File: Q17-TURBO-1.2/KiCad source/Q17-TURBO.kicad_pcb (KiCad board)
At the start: 2 copper layers, 190 x 75 mm, 106 parts, among them J1 INPUT, J2 SPK+, J3 DC, Q1 IRF610, Q10 KSA992, Q12 KSC1845, Q13 IRF610, Q14 IRF9610, Q15 FQA46N15, Q16 IXTH48P20P, Q17 FQA46N15, Q18 IXTH48P20P, Q2 KSA992, Q3 KSC1845, Q4 IRF9610, Q5 FQPF7P20, Q6 2SK3564, Q7 LSK170B, Q7' DN2540N8-G, Q8 DN2540, Q9 BS250P, T1 TestPoint_THTPad_D1.5mm_Drill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, T2 TestPoint_THTPad_D1.5mm_Drill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, T3 TestPoint_THTPad_D1.5mm_Drill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, T4 TestPoint_THTPad_D1.5mm_Drill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, T5 TestPoint_THTPad_D1.5mm_Drill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, T6 TestPoint_THTPad_D1.5mm_Drill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, U1 OPA1611, U1' OPA1641, U2 NDC7003P

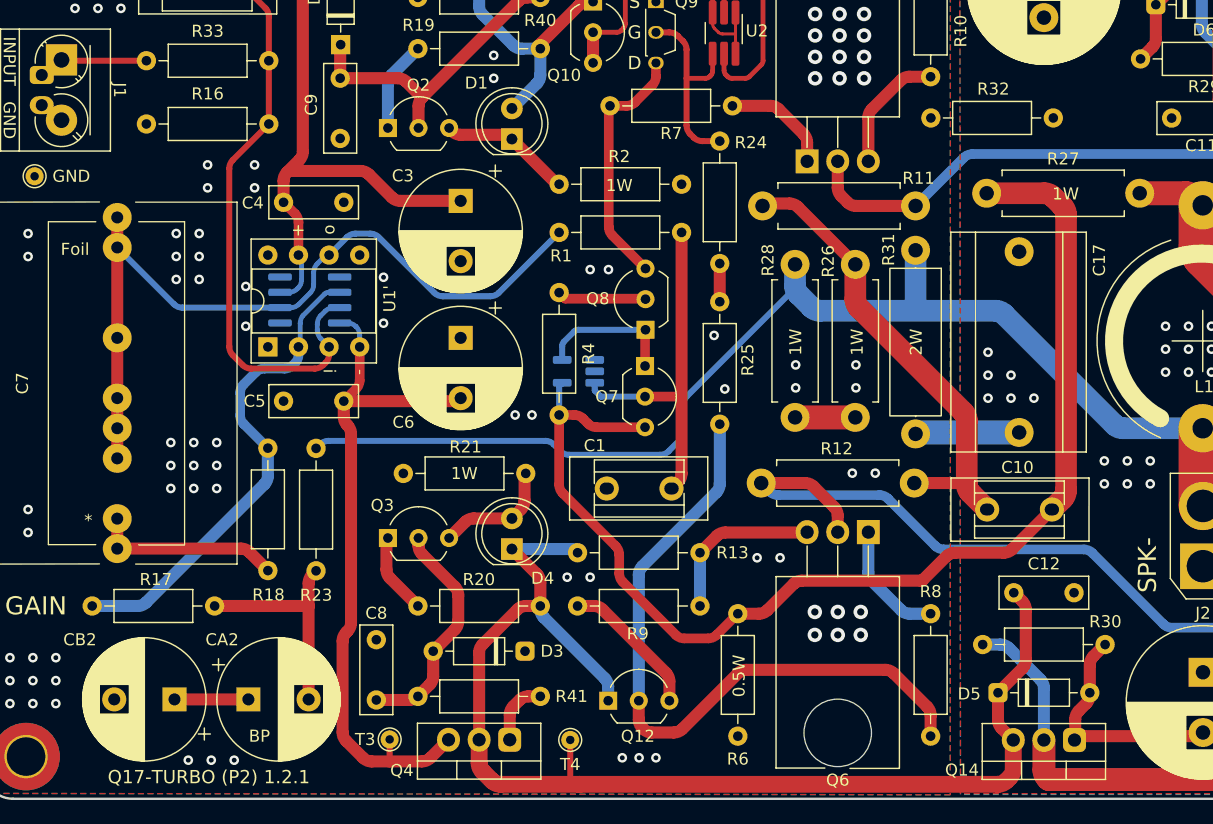
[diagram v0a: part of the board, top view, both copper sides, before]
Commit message: Update Q17-Turbo to 1.2.2
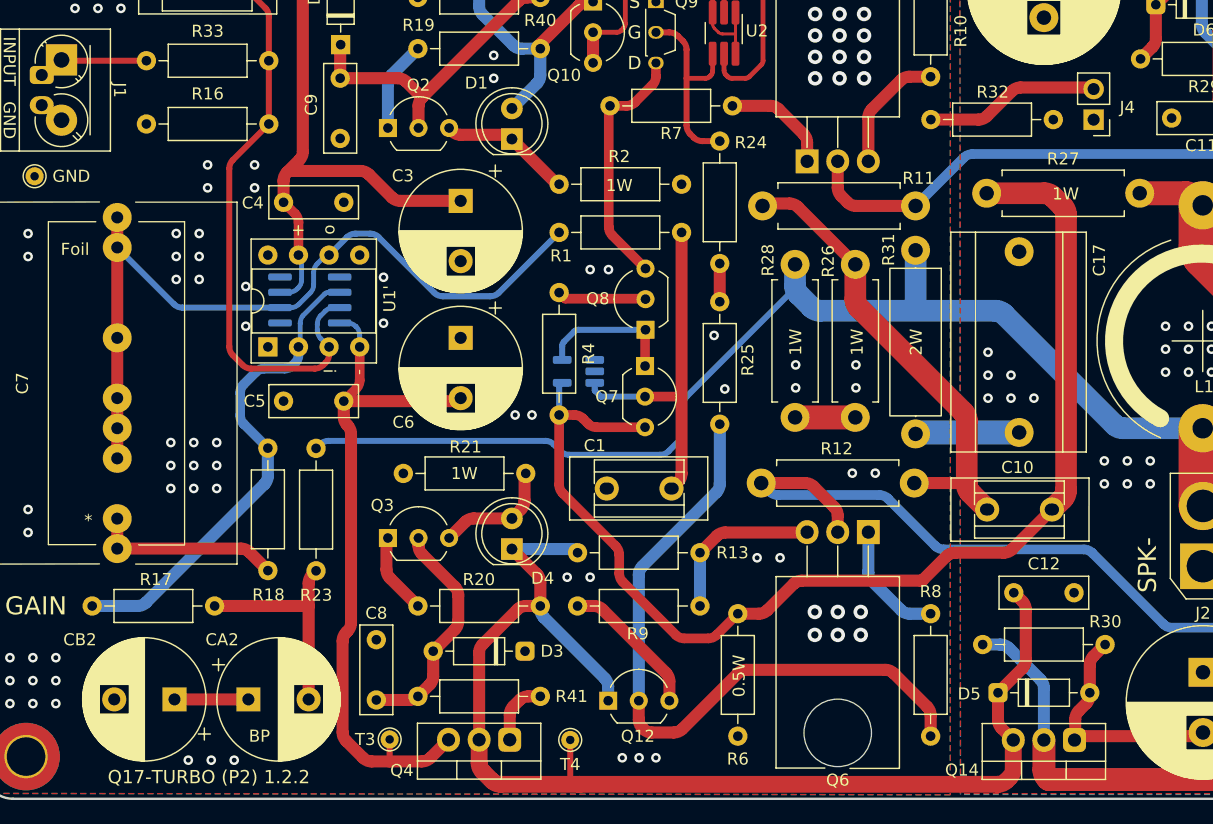
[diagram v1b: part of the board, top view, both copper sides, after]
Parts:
- added J4: PinHeader_1x02_P2.54mm_Vertical, Connector_PinHeader_2.54mm:PinHeader_1x02_P2.54mm_Vertical, F.Cu at (141.2, 89.8)
- moved R32 0.14 mm to (127.7, 89.8)
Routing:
- net GND: track 0.00 -> 14.4 mm
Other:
- board text added: "Q17-TURBO (P2) 1.2.2"
- board text removed: "Q17-TURBO (P2) 1.2.1"
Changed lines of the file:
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@@
   (title_block
     (title "Q17-TURBO (P2)")
-    (date "2023-08-06")
-    (rev "1.2.1")
+    (date "2023-09-04")
+    (rev "1.2.2")
     (company "PCB design by Stef")
     (comment 1 "Zize 190 x 75 mm")
@@
       (drillshape 0)
       (scaleselection 1)
-      (outputdirectory "../Gerber-Q17-TURBO 1.2.1")
+      (outputdirectory "../Gerber-Q17-TURBO 1.2.2")
     )
   )
@@
       (net 44 "Net-(Q4-S)"))
   )
+  (footprint "Connector_PinHeader_2.54mm:PinHeader_1x02_P2.54mm_Vertical" (layer "F.Cu")
+    (at 141.1732 89.7915 180)
+    (descr "Through hole straight pin header, 1x02, 2.54mm pitch, single row")
+    (tags "Through hole pin header THT 1x02 2.54mm single row")
+    (attr through_hole board_only)
+    (fp_text reference "J4" (at -2.794 1.021) (layer "F.SilkS")
+        (effects (font (size 1 1) (thickness 0.15)))
+    )
+    (fp_text value "PinHeader_1x02_P2.54mm_Vertical" (at 0 4.87) (layer "F.Fab")
+        (effects (font (size 1 1) (thickness 0.15)))
+    )
+    (fp_text user "${REFERENCE}" (at 0 1.27 90) (layer "F.Fab")
+        (effects (font (size 1 1) (thickness 0.15)))
+    )
+    (fp_line (start -1.33 -1.33) (end 0 -1.33)
+      (stroke (width 0.12) (type solid)) (layer "F.SilkS"))
+    (fp_line (start -1.33 0) (end -1.33 -1.33)
+      (stroke (width 0.12) (type solid)) (layer "F.SilkS"))
+    (fp_line (start -1.33 1.27) (end -1.33 3.87)
+      (stroke (width 0.12) (type solid)) (layer "F.SilkS"))
+    (fp_line (start -1.33 1.27) (end 1.33 1.27)
+      (stroke (width 0.12) (type solid)) (layer "F.SilkS"))
+    (fp_line (start -1.33 3.87) (end 1.33 3.87)
+      (stroke (width 0.12) (type solid)) (layer "F.SilkS"))
+    (fp_line (start 1.33 1.27) (end 1.33 3.87)
+      (stroke (width 0.12) (type solid)) (layer "F.SilkS"))
+    (fp_line (start -1.8 -1.8) (end -1.8 4.35)
+      (stroke (width 0.05) (type solid)) (layer "F.CrtYd"))
+    (fp_line (start -1.8 4.35) (end 1.8 4.35)
+      (stroke (width 0.05) (type solid)) (layer "F.CrtYd"))
+    (fp_line (start 1.8 -1.8) (end -1.8 -1.8)
+      (stroke (width 0.05) (type solid)) (layer "F.CrtYd"))
+    (fp_line (start 1.8 4.35) (end 1.8 -1.8)
+      (stroke (width 0.05) (type solid)) (layer "F.CrtYd"))
+    (fp_line (start -1.27 -0.635) (end -0.635 -1.27)
+      (stroke (width 0.1) (type solid)) (layer "F.Fab"))
+    (fp_line (start -1.27 3.81) (end -1.27 -0.635)
+      (stroke (width 0.1) (type solid)) (layer "F.Fab"))
+    (fp_line (start -0.635 -1.27) (end 1.27 -1.27)
+      (stroke (width 0.1) (type solid)) (layer "F.Fab"))
+    (fp_line (start 1.27 -1.27) (end 1.27 3.81)
+      (stroke (width 0.1) (type solid)) (layer "F.Fab"))
+    (fp_line (start 1.27 3.81) (end -1.27 3.81)
+      (stroke (width 0.1) (type solid)) (layer "F.Fab"))
+    (pad "1" thru_hole rect (at 0 0 180) (size 1.7 1.7) (drill 1) (layers "*.Cu" "*.Mask")
+      (net 4 "GNDPWR"))
+    (pad "2" thru_hole oval (at 0 2.54 180) (size 1.7 1.7) (drill 1) (layers "*.Cu" "*.Mask")
+      (net 1 "GND"))
+    (model "${KICAD6_3DMODEL_DIR}/Connector_PinHeader_2.54mm.3dshapes/PinHeader_1x02_P2.54mm_Vertical.wrl"
+      (offset (xyz 0 0 0))
+      (scale (xyz 1 1 1))
+      (rotate (xyz 0 0 0))
+    )
+  )
   (footprint "Resistor_THT:R_Axial_DIN0207_L6.3mm_D2.5mm_P10.16mm_Horizontal" (layer "F.Cu")
     (at 98.3472 130.15)
@@
     (descr "Resistor, Axial_DIN0207 series, Axial, Horizontal, pin pitch=10.16mm, 0.25W = 1/4W, length*diameter=6.3*2.5mm^2, http://cdn-reichelt.de/documents/datenblatt/B400/1_4W%23YAG.pdf")
     (tags "Resistor Axial_DIN0207 series Axial Horizontal pin pitch 10.16mm 0.25W = 1/4W length 6.3mm diameter 2.5mm")
-    (property "Mouser" "594-MRS25000C1009FRP")
-    (property "Part#" "MRS25000C1009FRP00")
+    (property "Mouser" "594-MRS2510K00F")
+    (property "Part#" "MRS25000C1002FRP00")
     (property "Sheetfile" "Q17-TURBO.kicad_sch")
     (property "Sheetname" "")
@@
   )
   (footprint "Resistor_THT:R_Axial_DIN0207_L6.3mm_D2.5mm_P10.16mm_Horizontal" (layer "F.Cu")
-    (at 127.6672 89.65)
+    (at 127.6672 89.7865)
     (descr "Resistor, Axial_DIN0207 series, Axial, Horizontal, pin pitch=10.16mm, 0.25W = 1/4W, length*diameter=6.3*2.5mm^2, http://cdn-reichelt.de/documents/datenblatt/B400/1_4W%23YAG.pdf")
     (tags "Resistor Axial_DIN0207 series Axial Horizontal pin pitch 10.16mm 0.25W = 1/4W length 6.3mm diameter 2.5mm")
@@
     (property "ki_keywords" "R res resistor")
     (attr through_hole)
-    (fp_text reference "R32" (at 5.18 -2.4) (layer "F.SilkS")
+    (fp_text reference "R32" (at 5.124 -2.286) (layer "F.SilkS")
         (effects (font (size 1 1) (thickness 0.15)))
     )
@@
     (effects (font (size 1 1) (thickness 0.15)))
   )
-  (gr_text "Q17-TURBO (P2) 1.2.1" (at 67.7472 144.35) (layer "F.SilkS")
+  (gr_text "Q17-TURBO (P2) 1.2.2" (at 67.7472 144.35) (layer "F.SilkS")
     (effects (font (size 1.1 1.1) (thickness 0.2)))
   )
@@
     (effects (font (size 1 1) (thickness 0.15)))
   )
+  (segment (start 141.0437 87.122) (end 135.107914 87.122) (width 1) (layer "F.Cu") (net 1))
+  (segment (start 134.400807 87.414893) (end 132.322093 89.493607) (width 1) (layer "F.Cu") (net 1))
+  (segment (start 131.614986 89.7865) (end 127.6672 89.7865) (width 1) (layer "F.Cu") (net 1))
   (via (at 67.9472 142.945) (size 0.8) (drill 0.4) (layers "F.Cu" "B.Cu") (free) (net 1))
   (via (at 91.3892 86.36) (size 0.8) (drill 0.4) (layers "F.Cu" "B.Cu") (free) (net 1))
@@
   (via (at 120.0912 86.36) (size 1.2) (drill 0.6) (layers "F.Cu" "B.Cu") (free) (net 1))
   (via (at 94.5642 114.3) (size 0.8) (drill 0.4) (layers "F.Cu" "B.Cu") (free) (net 1))
+  (arc (start 135.107914 87.122) (mid 134.725231 87.19812) (end 134.400807 87.414893) (width 1) (layer "F.Cu") (net 1))
+  (arc (start 131.614986 89.7865) (mid 131.997669 89.71038) (end 132.322093 89.493607) (width 1) (layer "F.Cu") (net 1))
   (segment (start 60.1472 125.3892) (end 60.1472 122.9) (width 1) (layer "F.Cu") (net 2))
   (segment (start 60.1472 125.3892) (end 70.412186 125.3892) (width 1) (layer "F.Cu") (net 2))

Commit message: Q17-Turbo: Update of R25 value.
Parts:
- R25: value 7k5 -> 8k2
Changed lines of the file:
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@@
   (title_block
     (title "Q17-TURBO (P2)")
-    (date "2023-09-05")
+    (date "2023-09-14")
     (rev "1.2.2")
     (company "PCB design by Stef")
@@
     (descr "Resistor, Axial_DIN0207 series, Axial, Horizontal, pin pitch=10.16mm, 0.25W = 1/4W, length*diameter=6.3*2.5mm^2, http://cdn-reichelt.de/documents/datenblatt/B400/1_4W%23YAG.pdf")
     (tags "Resistor Axial_DIN0207 series Axial Horizontal pin pitch 10.16mm 0.25W = 1/4W length 6.3mm diameter 2.5mm")
-    (property "Mouser" "594-MRS25000C7501FRP")
-    (property "Part#" "MRS25000C7501FRP00")
+    (property "Mouser" "594-MRS25000C8201FRP")
+    (property "Part#" "MRS25000C8201FRP00")
     (property "Sheetfile" "Q17-TURBO.kicad_sch")
     (property "Sheetname" "")
@@
         (effects (font (size 1 1) (thickness 0.15)))
     )
-    (fp_text value "7k5" (at 5.08 0.01 90) (layer "F.SilkS") hide
+    (fp_text value "8k2" (at 5.08 0.01 90) (layer "F.SilkS") hide
         (effects (font (size 1 1) (thickness 0.15)))
     )

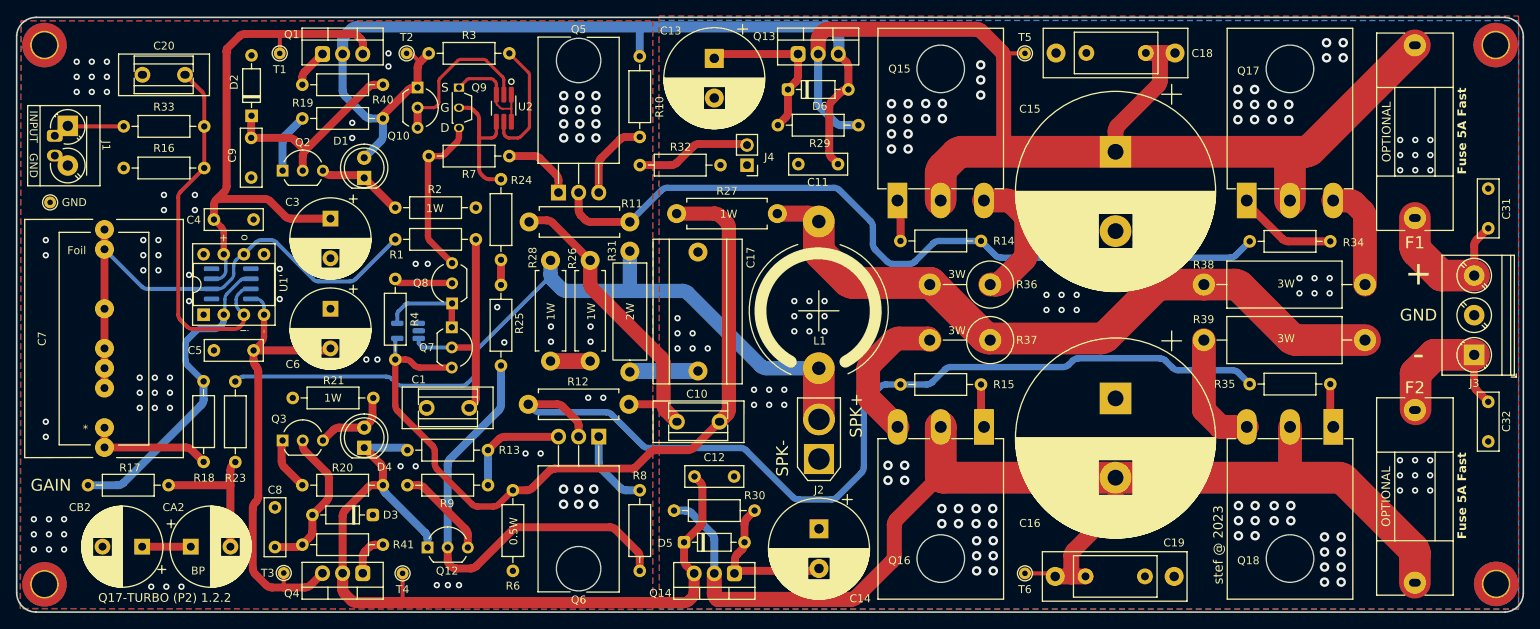
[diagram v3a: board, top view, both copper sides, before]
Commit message: Update Q17-Turbo to 1.2.3
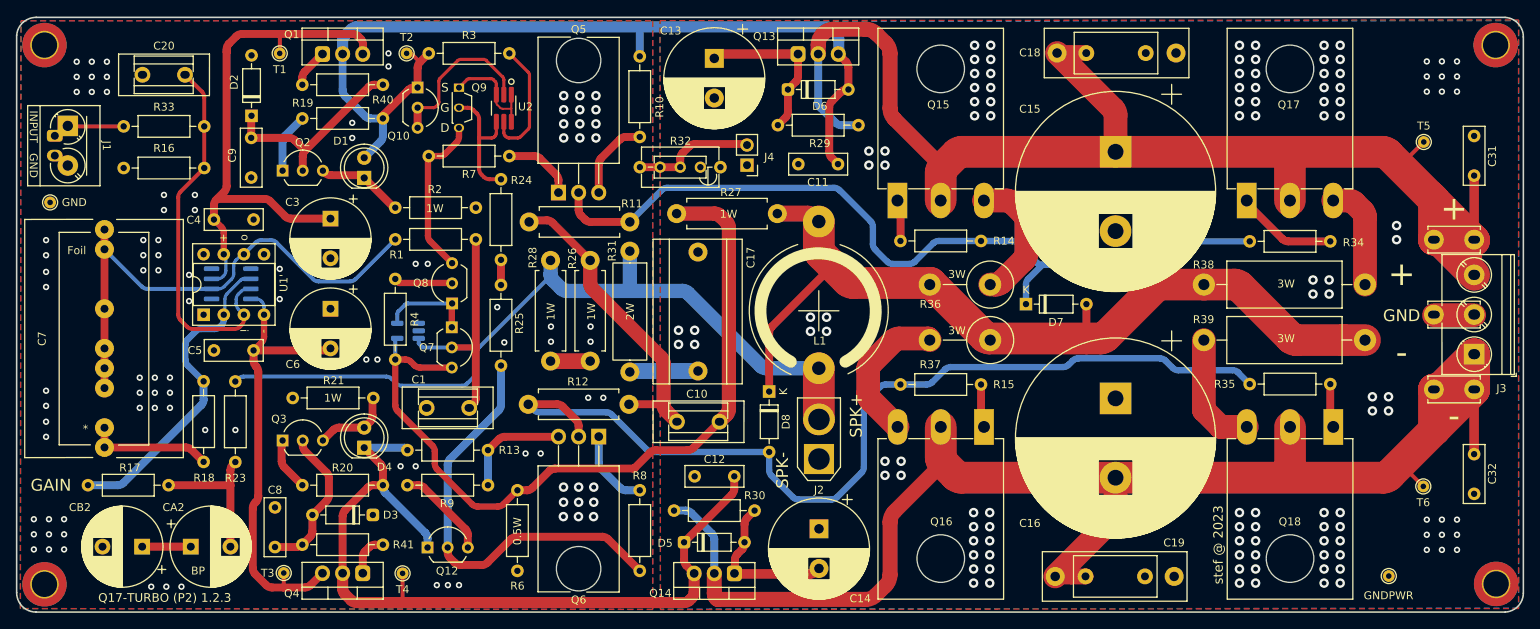
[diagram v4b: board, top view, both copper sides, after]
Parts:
- removed F1, F2: Fuse 5A Fast, Q17_Library:fuse_holder_CQ-2-Enlarged
- added D7: 1N5245B, Diode_THT:D_DO-35_SOD27_P7.62mm_Horizontal, F.Cu at (176.4, 107.3)
- added D8: 1N5245B, Diode_THT:D_DO-35_SOD27_P7.62mm_Horizontal, F.Cu at (144.0, 118.3)
- added T7: TestPoint_THTPad_D1.5mm_Drill0.7mm, TestPoint:TestPoint_THTPad_D1.5mm_Drill0.7mm, F.Cu at (222.1, 141.6)
- J3: footprint TerminalBlock_Phoenix:TerminalBlock_Phoenix_PT-1,5-3-5.0-H_1x03_P5.00mm_Horizontal -> Q17_Library:TerminalBlock_Phoenix_PT-1,5-3-5.0-H_1x03_P5.00mm_Horizontal_Faston
- R32: value STRAP -> 10R or STRAP J4; footprint Resistor_THT:R_Axial_DIN0207_L6.3mm_D2.5mm_P10.16mm_Horizontal -> Q17_Library:THT_POT_Vishay_T93Y_Vertical
- moved T5 51.5 mm to (226.5, 86.9)
- moved T6 51.4 mm to (226.5, 130.3)
- moved C18 15.1 mm to (195.3, 75.7), turned to 180 degrees
- moved C31 6.88 mm to (232.9, 86.1)
- moved C32 6.84 mm to (232.9, 131.2)
- moved C12 4.98 mm to (134.6, 129.0), turned to 0 degrees
- moved R6 0.57 mm to (112.2, 130.8)
- moved R32 0.26 mm to (127.7, 90.0)
- moved J3 0.09 mm to (232.9, 113.6)
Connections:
- C15 pad 1: Net-(Q13-D) -> Net-(J3-Pin_3)
- C16 pad 2: Net-(Q14-D) -> Net-(J3-Pin_1)
- C18 pad 2: Net-(Q13-D) -> Net-(J3-Pin_3)
- C19 pad 1: Net-(Q14-D) -> Net-(J3-Pin_1)
- Q13 pad 2: Net-(Q13-D) -> Net-(J3-Pin_3)
- Q14 pad 2: Net-(Q14-D) -> Net-(J3-Pin_1)
- Q15 pad 2: Net-(Q13-D) -> Net-(J3-Pin_3)
- Q16 pad 2: Net-(Q14-D) -> Net-(J3-Pin_1)
- Q17 pad 2: Net-(Q13-D) -> Net-(J3-Pin_3)
- Q18 pad 2: Net-(Q14-D) -> Net-(J3-Pin_1)
- R29 pad 1: Net-(Q13-D) -> Net-(J3-Pin_3)
- R30 pad 2: Net-(Q14-D) -> Net-(J3-Pin_1)
- T5 pad 1: Net-(Q13-D) -> Net-(J3-Pin_3)
- T6 pad 1: Net-(Q14-D) -> Net-(J3-Pin_1)
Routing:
- net Net-(J3-Pin_1): track 19.5 -> 200.1 mm
- net Net-(J3-Pin_3): track 19.4 -> 183.1 mm
- net Net-(Q14-D): track 153.7 -> 0.00 mm
- net Net-(Q13-D): track 147.3 -> 0.00 mm
- net Net-(D7-A): track 88.2 -> 111.7 mm
- net Net-(D7-K): track 97.6 -> 104.0 mm
- net GNDPWR: track 0.00 -> 5.07 mm
- net Net-(Q12-C): track 57.5 -> 54.4 mm
- net Net-(D8-A): track 117.9 -> 119.4 mm
- net Net-(D4-K): track 103.3 -> 104.6 mm
- net GND: track 14.4 -> 15.4 mm, vias 89 -> 98
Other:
- board text added: "GNDPWR"
- board text added: "Q17-TURBO (P2) 1.2.3"
- board text removed: "OPTIONAL"
- board text removed: "Q17-TURBO (P2) 1.2.2"
